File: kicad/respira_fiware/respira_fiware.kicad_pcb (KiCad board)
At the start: 4 copper layers, 71.7 x 76.7 mm, 17 parts, among them J1 AC PWR, J2 ES1-NO2, J3 SI7021, J4 RJ45, J5 SPS30, J6 DC PWR, U1 ESP32-NODEMCU, U2 myrra_48022

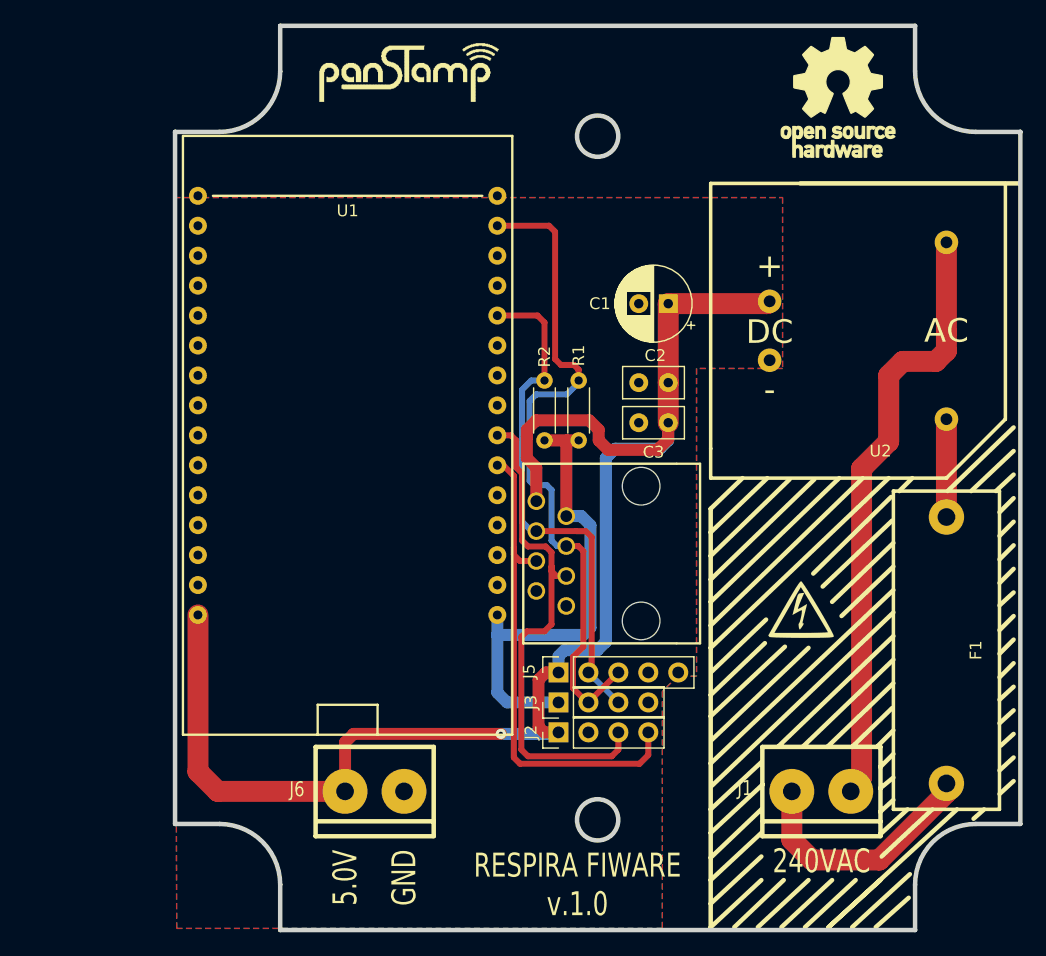
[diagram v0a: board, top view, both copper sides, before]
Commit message: Removing AC parts
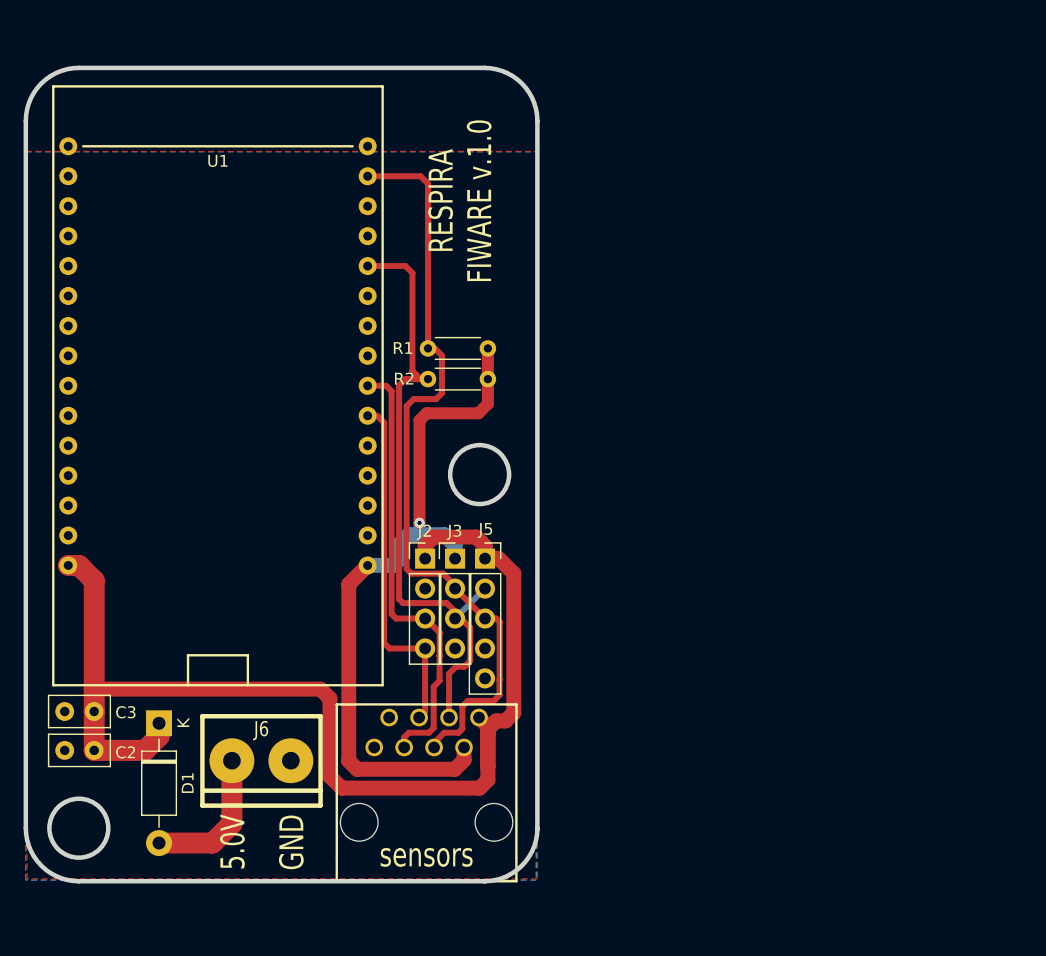
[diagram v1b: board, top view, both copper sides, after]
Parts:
- removed C1: 100u, Capacitor_THT:CP_Radial_D6.3mm_P2.50mm
- removed F1: 1A, mymods:litefuse_646
- removed the G*** at (134.6, 96.9)
- removed J1: AC PWR, myconnectors:terminal_block_5mm_2P
- removed U2: myrra_48022, mymods:myrra_48022
- added D1: 1N5817, Diode_THT:D_DO-41_SOD81_P10.16mm_Horizontal, F.Cu at (80.2, 106.6)
- C2: value 100n -> 1u
- G*** (x2): moved to B.Cu
- moved G*** 59.9 mm to (85.4, 82.5), turned to 180 degrees
- moved C2 57.8 mm to (74.7, 108.9)
- moved C3 54.5 mm to (74.7, 105.6)
- moved J4 29.2 mm to (102.9, 115.0), turned to 0 degrees
- moved G*** 21.3 mm to (92.7, 69.9), turned to 180 degrees
- moved J2 18.6 mm to (102.8, 92.6), turned to 0 degrees
- moved J3 15.0 mm to (105.3, 92.6), turned to 0 degrees
- moved U1 11.8 mm to (85.2, 76.7)
- moved J5 11.5 mm to (107.9, 92.6), turned to 0 degrees
- moved R1 11.0 mm to (108.1, 74.8), turned to 180 degrees
- moved J6 9.95 mm to (88.9, 109.8)
- moved R2 7.08 mm to (108.1, 77.4), turned to 180 degrees
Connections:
- J6 pad 1: +5V -> Net-(D1-Pad2)
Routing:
- net Net-(J1-Pad2): track 51.6 -> 0.00 mm
- net +5V: track 126.7 -> 99.8 mm, vias 1 -> 0
- net Net-(F1-Pad1): track 21.1 -> 0.00 mm
- net +3V3: track 40.7 -> 60.3 mm, vias 0 -> 1
- net Net-(D1-Pad2): track 0.00 -> 12.2 mm
- net /RXD2: track 42.3 -> 30.1 mm
- net /I2C_SDA: track 44.2 -> 54.5 mm
- net Net-(F1-Pad2): track 8.30 -> 0.00 mm
- net /I2C_SCL: track 58.4 -> 66.1 mm
- net /TXD2: track 44.1 -> 37.8 mm
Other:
- board size 71.7 x 76.7 mm -> 43.4 x 69 mm
- board text added: "sensors"
- board text removed: "240VAC"

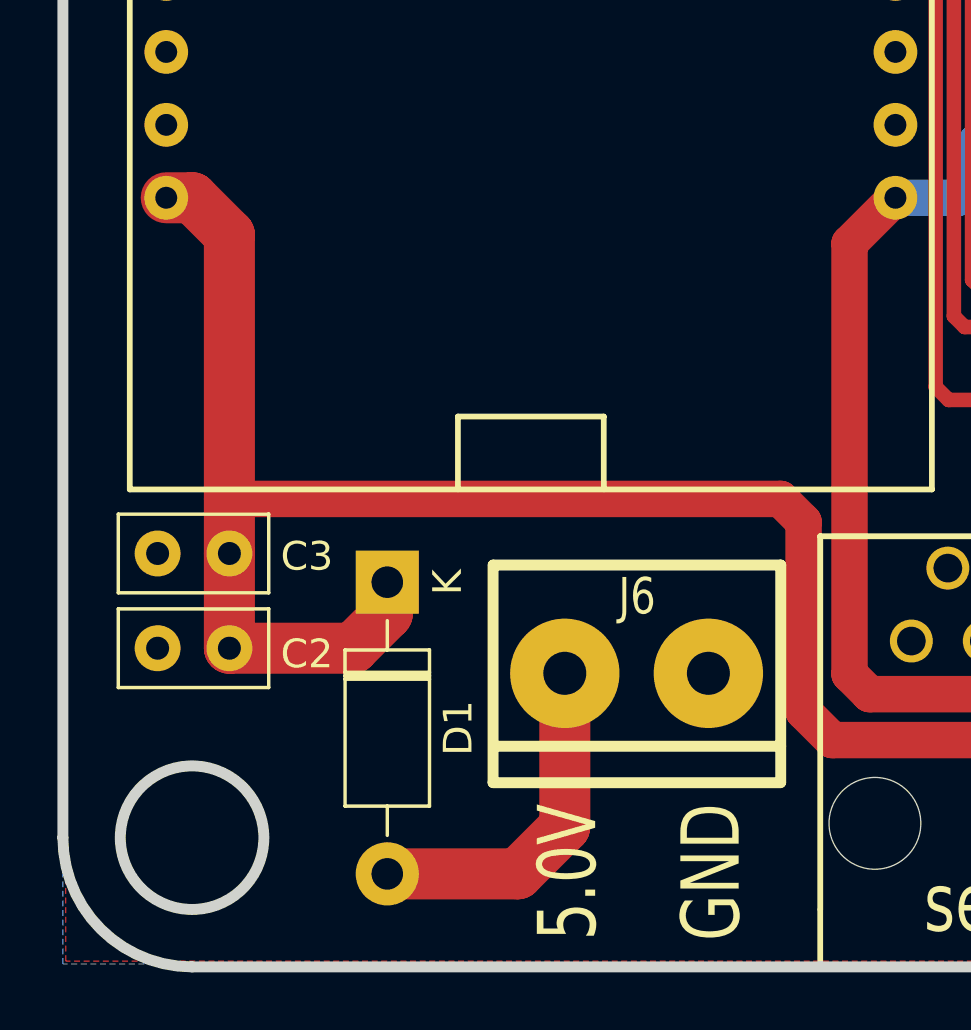
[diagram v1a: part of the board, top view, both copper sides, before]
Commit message: D1 removed
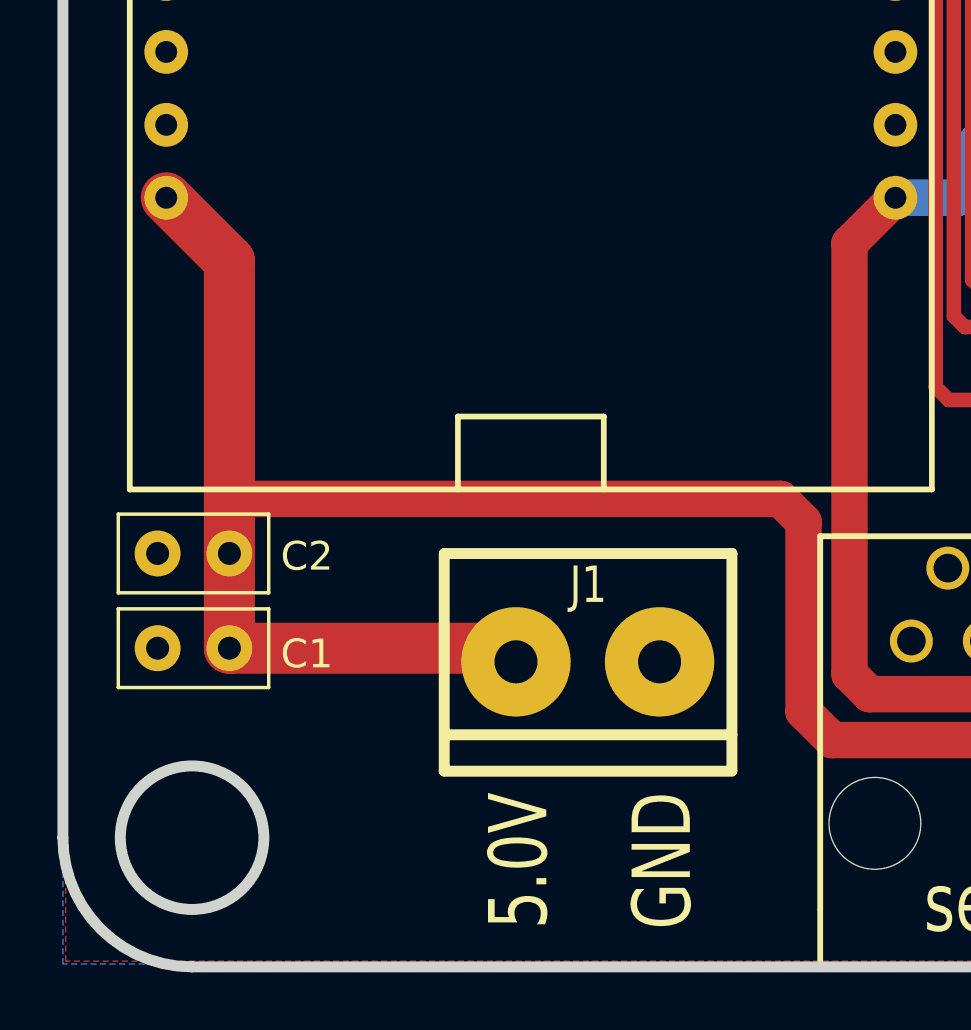
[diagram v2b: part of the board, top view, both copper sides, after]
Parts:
- removed C3: 100n, Capacitor_THT:C_Disc_D5.0mm_W2.5mm_P2.50mm
- removed D1: 1N5817, Diode_THT:D_DO-41_SOD81_P10.16mm_Horizontal
- added C1: 1u, Capacitor_THT:C_Disc_D5.0mm_W2.5mm_P2.50mm, F.Cu at (74.7, 108.9)
- C2: value 1u -> 100n
- moved C2 3.30 mm to (74.7, 105.6)
- moved J1 1.75 mm to (87.2, 109.4)
- renumbered J6 to J1
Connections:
- J1 pad 1: Net-(D1-Pad2) -> +5V
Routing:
- net Net-(D1-Pad2): track 12.2 -> 0.00 mm
- net +5V: track 99.8 -> 102.4 mm
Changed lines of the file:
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@@
     (thickness 1.6002)
     (drawings 14)
-    (tracks 128)
+    (tracks 124)
     (zones 0)
-    (modules 13)
-    (nets 31)
+    (modules 12)
+    (nets 30)
   )
   (page A4)
@@
   )
   (setup
-    (last_trace_width 1.27)
+    (last_trace_width 1.778)
     (user_trace_width 0.2032)
     (user_trace_width 0.254)
@@
   (net 28 /TXD0)
   (net 29 "Net-(U1-Pad30)")
-  (net 30 "Net-(D1-Pad2)")
   (net_class Default "This is the default net class."
     (clearance 0.127)
@@
     (add_net /TXD2)
     (add_net GND)
-    (add_net "Net-(D1-Pad2)")
     (add_net "Net-(U1-Pad1)")
     (add_net "Net-(U1-Pad10)")
@@
   )
   (module myconnectors:terminal_block_5mm_2P (layer Front)
-    (at 88.9 109.8)
+    (at 87.2 109.4)
     (descr "Bornier d'alimentation 4 pins")
     (tags DEV)
-    (fp_text reference J6 (at 0 -2.7) (layer F.SilkS)
+    (fp_text reference J1 (at 0 -2.7) (layer F.SilkS)
       (effects (font (size 1.27 1.016) (thickness 0.1524)))
     )
@@
     (fp_line (start -5.0165 3.7719) (end -5.0165 -3.7973) (layer F.SilkS) (width 0.381))
     (pad 1 thru_hole circle (at -2.51714 -0.0254) (size 3.81 3.81) (drill 1.4986) (layers *.Cu *.Mask F.SilkS)
-      (net 30 "Net-(D1-Pad2)"))
+      (net 1 +5V))
     (pad 2 thru_hole circle (at 2.48412 -0.0254) (size 3.81 3.81) (drill 1.4986) (layers *.Cu *.Mask F.SilkS)
       (net 2 GND))
@@
     (descr "C, Disc series, Radial, pin pitch=2.50mm, , diameter*width=5*2.5mm^2, Capacitor, http://cdn-reichelt.de/documents/datenblatt/B300/DS_KERKO_TC.pdf")
     (tags "C Disc series Radial pin pitch 2.50mm  diameter 5mm width 2.5mm Capacitor")
-    (fp_text reference C2 (at -2.7 -0.2 180) (layer F.SilkS)
+    (fp_text reference C1 (at -2.7 -0.2 180) (layer F.SilkS)
       (effects (font (size 1 1) (thickness 0.15)))
     )
@@
     (descr "C, Disc series, Radial, pin pitch=2.50mm, , diameter*width=5*2.5mm^2, Capacitor, http://cdn-reichelt.de/documents/datenblatt/B300/DS_KERKO_TC.pdf")
     (tags "C Disc series Radial pin pitch 2.50mm  diameter 5mm width 2.5mm Capacitor")
-    (fp_text reference C3 (at -2.7 -0.1 180) (layer F.SilkS)
+    (fp_text reference C2 (at -2.7 -0.1 180) (layer F.SilkS)
       (effects (font (size 1 1) (thickness 0.15)))
     )
@@
       (xy -3.012107 -4.689475) (xy -3.007963 -5.08)) (layer B.SilkS) (width 0.1))
   )
-  (module Diode_THT:D_DO-41_SOD81_P10.16mm_Horizontal (layer Front)
-    (at 80.2 106.6 270)
-    (descr "Diode, DO-41_SOD81 series, Axial, Horizontal, pin pitch=10.16mm, , length*diameter=5.2*2.7mm^2, , http://www.diodes.com/_files/packages/DO-41%20(Plastic).pdf")
-    (tags "Diode DO-41_SOD81 series Axial Horizontal pin pitch 10.16mm  length 5.2mm diameter 2.7mm")
-    (fp_text reference D1 (at 5.08 -2.47 270) (layer F.SilkS)
-      (effects (font (size 1 1) (thickness 0.15)))
-    )
-    (fp_text value 1N5817 (at 5.08 2.47 270) (layer F.Fab)
-      (effects (font (size 1 1) (thickness 0.15)))
-    )
-    (fp_line (start 2.48 -1.35) (end 2.48 1.35) (layer F.Fab) (width 0.1))
-    (fp_line (start 2.48 1.35) (end 7.68 1.35) (layer F.Fab) (width 0.1))
-    (fp_line (start 7.68 1.35) (end 7.68 -1.35) (layer F.Fab) (width 0.1))
-    (fp_line (start 7.68 -1.35) (end 2.48 -1.35) (layer F.Fab) (width 0.1))
-    (fp_line (start 0 0) (end 2.48 0) (layer F.Fab) (width 0.1))
-    (fp_line (start 10.16 0) (end 7.68 0) (layer F.Fab) (width 0.1))
-    (fp_line (start 3.26 -1.35) (end 3.26 1.35) (layer F.Fab) (width 0.1))
-    (fp_line (start 3.36 -1.35) (end 3.36 1.35) (layer F.Fab) (width 0.1))
-    (fp_line (start 3.16 -1.35) (end 3.16 1.35) (layer F.Fab) (width 0.1))
-    (fp_line (start 2.36 -1.47) (end 2.36 1.47) (layer F.SilkS) (width 0.12))
-    (fp_line (start 2.36 1.47) (end 7.8 1.47) (layer F.SilkS) (width 0.12))
-    (fp_line (start 7.8 1.47) (end 7.8 -1.47) (layer F.SilkS) (width 0.12))
-    (fp_line (start 7.8 -1.47) (end 2.36 -1.47) (layer F.SilkS) (width 0.12))
-    (fp_line (start 1.34 0) (end 2.36 0) (layer F.SilkS) (width 0.12))
-    (fp_line (start 8.82 0) (end 7.8 0) (layer F.SilkS) (width 0.12))
-    (fp_line (start 3.26 -1.47) (end 3.26 1.47) (layer F.SilkS) (width 0.12))
-    (fp_line (start 3.38 -1.47) (end 3.38 1.47) (layer F.SilkS) (width 0.12))
-    (fp_line (start 3.14 -1.47) (end 3.14 1.47) (layer F.SilkS) (width 0.12))
-    (fp_line (start -1.35 -1.6) (end -1.35 1.6) (layer F.CrtYd) (width 0.05))
-    (fp_line (start -1.35 1.6) (end 11.51 1.6) (layer F.CrtYd) (width 0.05))
-    (fp_line (start 11.51 1.6) (end 11.51 -1.6) (layer F.CrtYd) (width 0.05))
-    (fp_line (start 11.51 -1.6) (end -1.35 -1.6) (layer F.CrtYd) (width 0.05))
-    (fp_text user %R (at 5.47 0 270) (layer F.Fab)
-      (effects (font (size 1 1) (thickness 0.15)))
-    )
-    (fp_text user K (at 0 -2.1 270) (layer F.Fab)
-      (effects (font (size 1 1) (thickness 0.15)))
-    )
-    (fp_text user K (at 0 -2.1 270) (layer F.SilkS)
-      (effects (font (size 1 1) (thickness 0.15)))
-    )
-    (pad 1 thru_hole rect (at 0 0 270) (size 2.2 2.2) (drill 1.1) (layers *.Cu *.Mask)
-      (net 1 +5V))
-    (pad 2 thru_hole oval (at 10.16 0 270) (size 2.2 2.2) (drill 1.1) (layers *.Cu *.Mask)
-      (net 30 "Net-(D1-Pad2)"))
-    (model ${KISYS3DMOD}/Diode_THT.3dshapes/D_DO-41_SOD81_P10.16mm_Horizontal.wrl
-      (at (xyz 0 0 0))
-      (scale (xyz 1 1 1))
-      (rotate (xyz 0 0 0))
-    )
-  )
   (gr_line (start 73.4 120) (end 107.9 120) (layer Edge.Cuts) (width 0.381))
   (gr_line (start 73.4 51) (end 107.8 51) (layer Edge.Cuts) (width 0.381))
@@
   (gr_circle (center 73.4 115.5) (end 75.9 115.5) (layer Edge.Cuts) (width 0.381))
   (gr_circle (center 107.4 85.5) (end 109.9 85.5) (layer Edge.Cuts) (width 0.381))
-  (gr_text GND (at 91.5 116.7 90) (layer F.SilkS)
+  (gr_text GND (at 89.8 116.3 90) (layer F.SilkS)
     (effects (font (size 2.032 1.524) (thickness 0.3048)))
   )
-  (gr_text 5.0V (at 86.5 116.7 90) (layer F.SilkS)
+  (gr_text 5.0V (at 84.8 116.3 90) (layer F.SilkS)
     (effects (font (size 2.032 1.524) (thickness 0.3048)))
   )
@@
     (effects (font (size 2.032 1.524) (thickness 0.3048)))
   )
-  (segment (start 74.7 108.9) (end 79 108.9) (width 1.778) (layer Front) (net 1))
-  (segment (start 80.2 107.7) (end 80.2 106.6) (width 1.778) (layer Front) (net 1))
-  (segment (start 79 108.9) (end 80.2 107.7) (width 1.778) (layer Front) (net 1))
   (segment (start 74.7 108.9) (end 74.7 105.6) (width 1.778) (layer Front) (net 1))
-  (segment (start 73.41 93.21) (end 72.5 93.21) (width 1.778) (layer Front) (net 1))
-  (segment (start 74.7 94.5) (end 73.41 93.21) (width 1.778) (layer Front) (net 1))
-  (segment (start 74.7 103.7) (end 93.9 103.7) (width 1.27) (layer Front) (net 1))
-  (segment (start 74.7 103.7) (end 74.7 94.5) (width 1.778) (layer Front) (net 1))
-  (segment (start 74.7 105.6) (end 74.7 103.7) (width 1.778) (layer Front) (net 1))
   (segment (start 93.9 103.7) (end 94.7 104.5) (width 1.27) (layer Front) (net 1))
   (segment (start 94.7 104.5) (end 94.7 111.1) (width 1.27) (layer Front) (net 1))
@@
   (segment (start 109.032448 92.632448) (end 110.3 93.9) (width 1.27) (layer Front) (net 1))
   (segment (start 109.6 106.4) (end 108.8 106.4) (width 1.27) (layer Front) (net 1))
+  (segment (start 74.7 95.41) (end 72.5 93.21) (width 1.778) (layer Front) (net 1))
+  (segment (start 74.8 103.7) (end 74.7 103.8) (width 1.27) (layer Front) (net 1))
+  (segment (start 93.9 103.7) (end 74.8 103.7) (width 1.27) (layer Front) (net 1))
+  (segment (start 74.7 105.6) (end 74.7 103.8) (width 1.778) (layer Front) (net 1))
+  (segment (start 74.7 103.8) (end 74.7 95.41) (width 1.778) (layer Front) (net 1))
+  (segment (start 84.20826 108.9) (end 84.68286 109.3746) (width 1.778) (layer Front) (net 1))
+  (segment (start 74.7 108.9) (end 84.20826 108.9) (width 1.778) (layer Front) (net 1))
   (segment (start 97.9 93.21) (end 97.89 93.21) (width 1.27) (layer Front) (net 3))
   (segment (start 97.89 93.21) (end 96.3 94.8) (width 1.27) (layer Front) (net 3))
@@
   (segment (start 106.6 101.3) (end 106.1 101.8) (width 0.508) (layer Front) (net 8))
   (segment (start 106.1 101.8) (end 105.4 101.8) (width 0.508) (layer Front) (net 8))
-  (segment (start 80.2 116.76) (end 84.74 116.76) (width 1.778) (layer Front) (net 30))
-  (segment (start 86.38286 115.11714) (end 86.38286 109.7746) (width 1.778) (layer Front) (net 30))
-  (segment (start 84.74 116.76) (end 86.38286 115.11714) (width 1.778) (layer Front) (net 30))
   (zone (net 2) (net_name GND) (layer Back) (hatch edge 0.508)
     (connect_pads (clearance 0.1524))

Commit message: Minor arrangements
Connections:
- J3 pad 1: +3V3 -> Net-(J3-Pad1)
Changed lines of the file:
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@@
     (zones 0)
     (modules 12)
-    (nets 30)
+    (nets 31)
   )
   (page A4)
@@
   )
   (setup
-    (last_trace_width 1.778)
+    (last_trace_width 0.1524)
     (user_trace_width 0.2032)
     (user_trace_width 0.254)
@@
   (net 28 /TXD0)
   (net 29 "Net-(U1-Pad30)")
+  (net 30 "Net-(J3-Pad1)")
   (net_class Default "This is the default net class."
     (clearance 0.127)
@@
     (add_net /TXD2)
     (add_net GND)
+    (add_net "Net-(J3-Pad1)")
     (add_net "Net-(U1-Pad1)")
     (add_net "Net-(U1-Pad10)")
@@
     )
     (pad 1 thru_hole rect (at 0 0) (size 1.7 1.7) (drill 1) (layers *.Cu *.Mask)
-      (net 3 +3V3))
+      (net 30 "Net-(J3-Pad1)"))
     (pad 2 thru_hole oval (at 0 2.54) (size 1.7 1.7) (drill 1) (layers *.Cu *.Mask)
       (net 7 /I2C_SCL))

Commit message: Preparing for production
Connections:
- J3 pad 1: Net-(J3-Pad1) -> +3V3
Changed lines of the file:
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@@
     (zones 0)
     (modules 12)
-    (nets 31)
+    (nets 30)
   )
   (page A4)
@@
     (visible_elements FFFFF7BF)
     (pcbplotparams
-      (layerselection 0x010e0_fffffff9)
+      (layerselection 0x010f0_fffffff9)
       (usegerberextensions false)
       (usegerberattributes false)
@@
   (net 28 /TXD0)
   (net 29 "Net-(U1-Pad30)")
-  (net 30 "Net-(J3-Pad1)")
   (net_class Default "This is the default net class."
     (clearance 0.127)
@@
     (add_net /TXD2)
     (add_net GND)
-    (add_net "Net-(J3-Pad1)")
     (add_net "Net-(U1-Pad1)")
     (add_net "Net-(U1-Pad10)")
@@
     )
     (pad 1 thru_hole rect (at 0 0) (size 1.7 1.7) (drill 1) (layers *.Cu *.Mask)
-      (net 30 "Net-(J3-Pad1)"))
+      (net 3 +3V3))
     (pad 2 thru_hole oval (at 0 2.54) (size 1.7 1.7) (drill 1) (layers *.Cu *.Mask)
       (net 7 /I2C_SCL))
